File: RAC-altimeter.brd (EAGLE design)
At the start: 160 x 100 mm, 30 parts, among them J3 CORTEX_DEBUG_SMD, U1 MAX32660GTP+, U2 BMI088, U3 BMP388, U4 W25N01GVZEIG_TR, Y1 32.768kHz

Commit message: Organized board for layout
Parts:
- moved R2 104.5 mm to (62.2, 27.9)
- moved C2 103.2 mm to (54.6, 63.5)
- moved D1 101.7 mm to (61.0, 24.1)
- moved R1 100.5 mm to (62.2, 30.5)
- moved C1 98.8 mm to (54.6, 61.0)
- moved U1 95.2 mm to (53.3, 25.4)
- moved U3 95.2 mm to (59.7, 62.2)
- moved Y1 91.5 mm to (57.1, 34.3)
- moved R6 90.0 mm to (59.7, 66.0)
- moved U4 89.8 mm to (52.1, 5.08)
- moved R4 87.3 mm to (67.3, 27.9)
- moved C8 86.8 mm to (48.3, 10.2)
- moved R5 86.0 mm to (61.0, 21.6)
- moved R3 83.2 mm to (67.3, 30.5)
- moved C4 82.7 mm to (62.2, 52.1)
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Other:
- board size 160 x 100 mm -> 25.4 x 50.8 mm

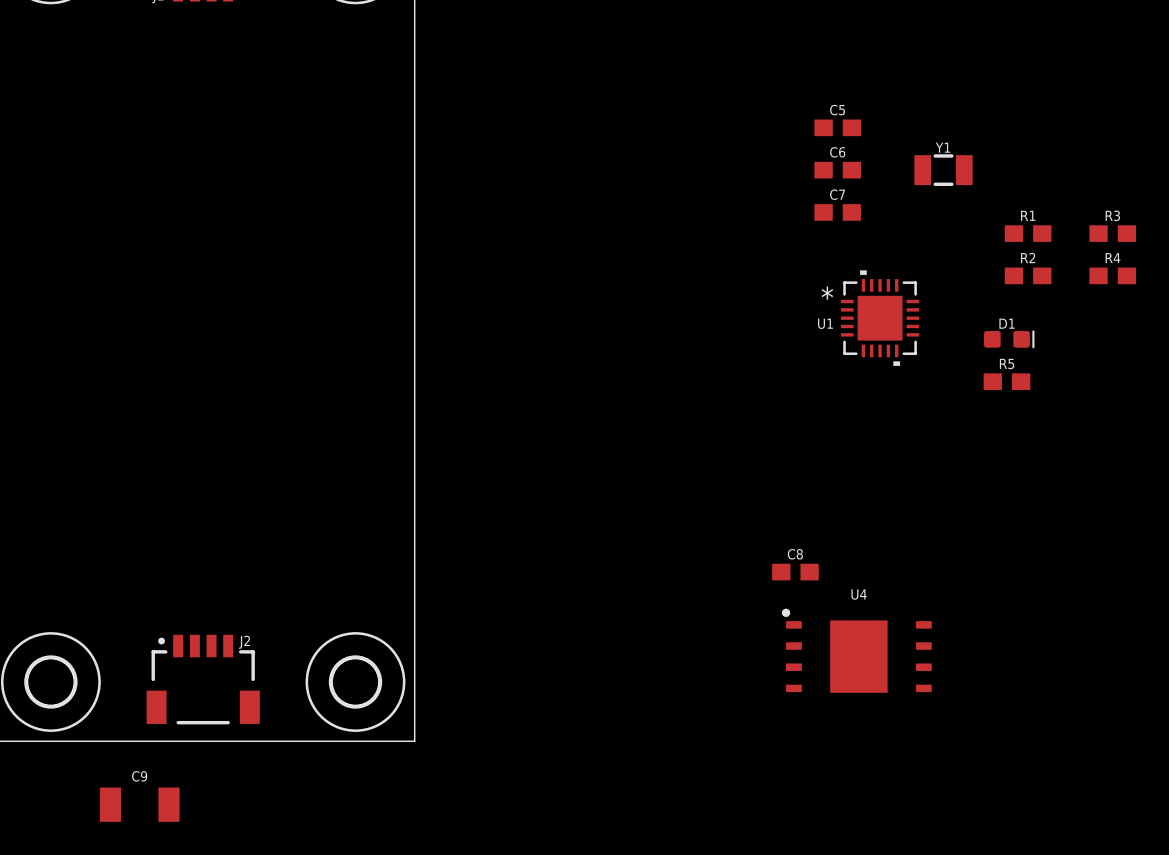
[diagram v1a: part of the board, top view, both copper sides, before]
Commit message: Swapped I2C0 and I2C1 bus connections for better routing
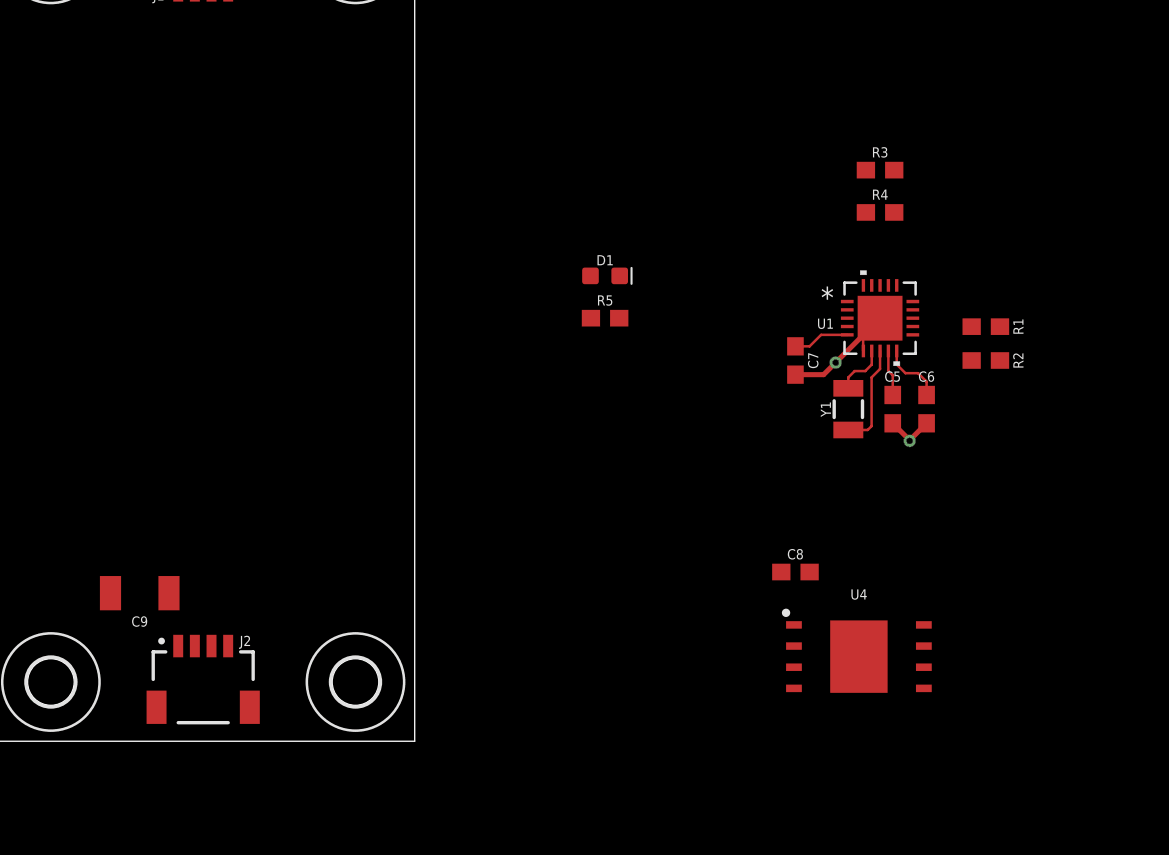
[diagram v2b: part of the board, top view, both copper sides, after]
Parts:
- moved D1 24.4 mm to (36.8, 27.9)
- moved R5 24.4 mm to (36.8, 25.4)
- moved C5 17.2 mm to (54.1, 19.9), turned to 270 degrees
- moved Y1 15.4 mm to (51.4, 19.9), turned to 90 degrees
- moved C6 15.3 mm to (56.1, 19.9), turned to 270 degrees
- moved R3 14.5 mm to (53.3, 34.3)
- moved R4 14.5 mm to (53.3, 31.8)
- moved C9 12.7 mm to (8.89, 8.89), turned to 180 degrees
- moved C7 9.25 mm to (48.3, 22.9), turned to 270 degrees
- moved R1 6.14 mm to (59.7, 24.9)
- moved R2 5.68 mm to (59.7, 22.9)
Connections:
- net I2C0_SCL: now also J1.4, J2.4; no longer U2.8, U3.2
- net I2C0_SDA: now also J1.3, J2.3; no longer U2.9, U3.4
- net I2C1_SCL: now also U2.8, U3.2; no longer J1.4, J2.4
- net I2C1_SDA: now also U2.9, U3.4; no longer J1.3, J2.3
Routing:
- net GND: track 0.00 -> 11.9 mm, vias 0 -> 2
- net 32KIN: track 0.00 -> 6.21 mm
- net VCORE: track 0.00 -> 3.83 mm
- net !RSTN: track 0.00 -> 3.40 mm
- net 32KOUT: track 0.00 -> 3.20 mm
- net VCC: track 0.00 -> 2.75 mm

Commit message: Partially routed board
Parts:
- moved R6 65.0 mm to (8.00, 26.7), turned to 90 degrees
- moved U3 64.8 mm to (5.33, 26.9), turned to 90 degrees
- moved C2 63.7 mm to (2.67, 26.7), turned to 270 degrees
- moved C1 58.4 mm to (5.33, 29.6)
- moved C4 55.1 mm to (8.89, 38.1), turned to 270 degrees
- moved C3 48.6 mm to (16.5, 38.1), turned to 270 degrees
- moved J4 46.4 mm to (26.7, 14.1), turned to 270 degrees
- moved U2 45.4 mm to (12.7, 38.1), turned to 270 degrees
- moved U4 42.1 mm to (15.2, 25.4)
- moved Y1 39.6 mm to (12.4, 12.8), turned to 180 degrees
- moved U1 38.9 mm to (15.2, 17.8)
- moved C7 38.7 mm to (10.2, 16.1)
- moved C5 38.4 mm to (16.5, 12.3)
- moved C6 38.2 mm to (18.7, 12.3)
- moved C8 36.8 mm to (17.1, 29.7), turned to 180 degrees
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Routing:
- net I2C0_SCL: track 0.00 -> 63.5 mm, vias 0 -> 3
- net I2C0_SDA: track 0.00 -> 55.5 mm, vias 0 -> 3
- net GND: track 11.9 -> 48.8 mm, vias 2 -> 12
- net VCC: track 2.75 -> 19.5 mm
- net !RSTN: track 3.40 -> 17.9 mm
- net !SPI0_CS: track 0.00 -> 14.3 mm, vias 0 -> 2
- net SPI0_MISO: track 0.00 -> 9.22 mm
- net SPI0_SCK: track 0.00 -> 8.88 mm
- net SWDCLK: track 0.00 -> 7.54 mm, vias 0 -> 2
- net UART1_TX: track 0.00 -> 7.52 mm, vias 0 -> 1
- net SWDIO: track 0.00 -> 7.01 mm
- net UART1_RX: track 0.00 -> 5.70 mm
- net SPI0_MOSI: track 0.00 -> 5.65 mm
- net 32KOUT: track 3.20 -> 5.94 mm
- net BMP_CS: track 0.00 -> 2.26 mm
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
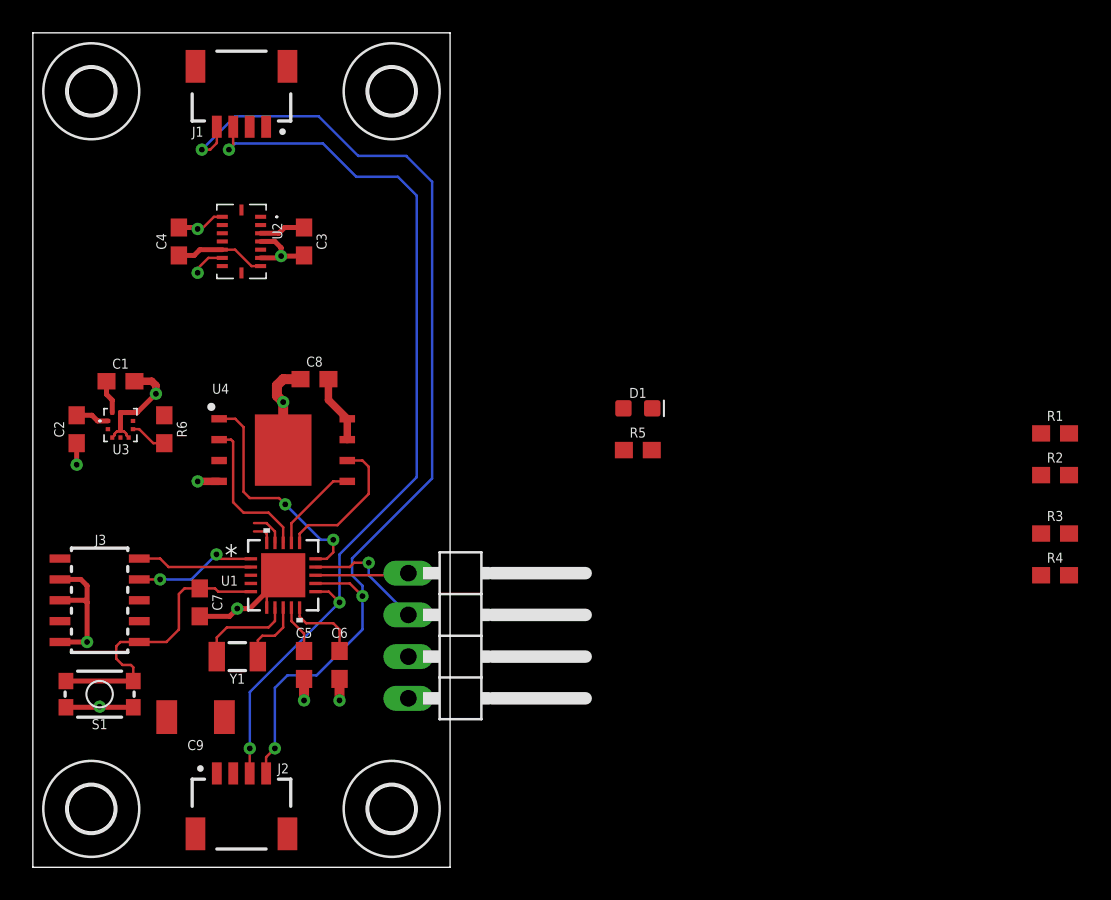
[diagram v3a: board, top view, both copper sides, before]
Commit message: Completely routed board
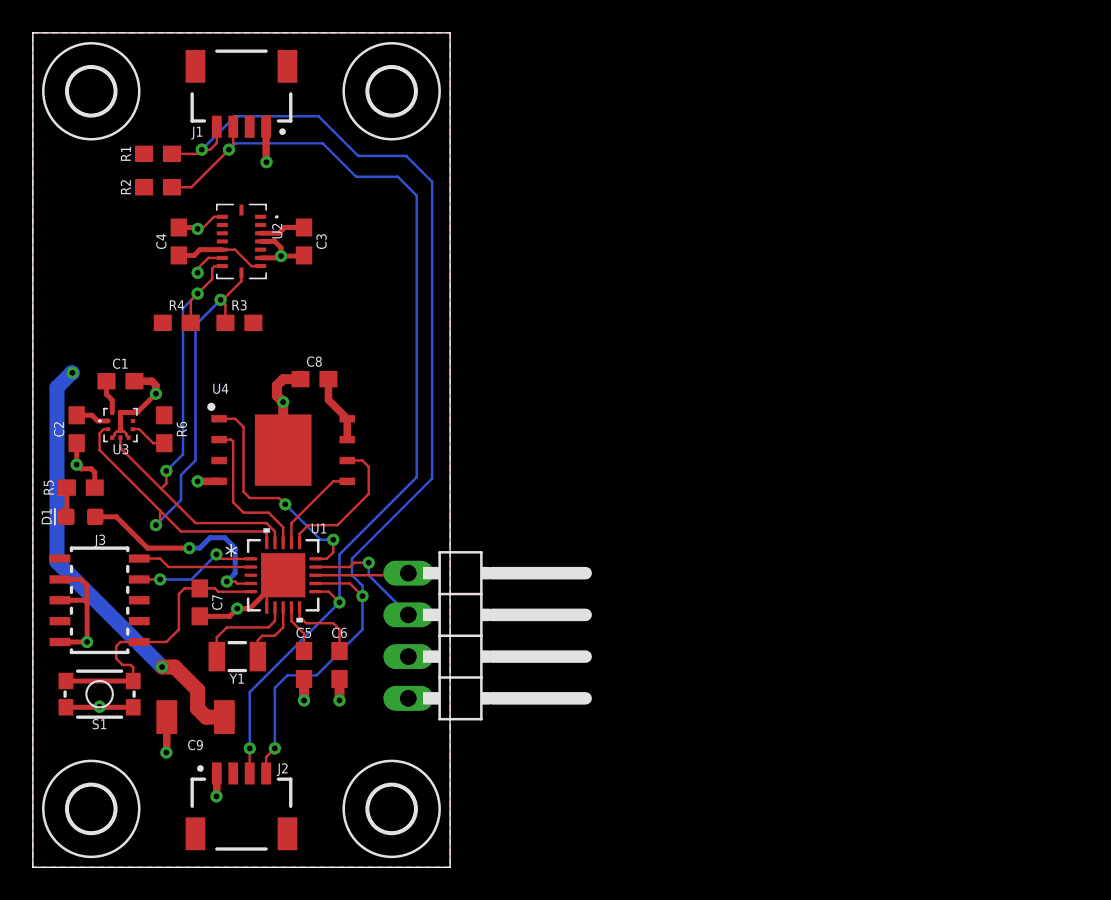
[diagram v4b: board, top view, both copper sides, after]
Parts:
- moved R2 57.4 mm to (7.62, 41.4), turned to 180 degrees
- moved R1 57.2 mm to (7.62, 43.4), turned to 180 degrees
- moved R4 55.6 mm to (8.76, 33.1), turned to 180 degrees
- moved R3 51.3 mm to (12.6, 33.1)
- moved D1 34.5 mm to (2.92, 21.3), turned to 180 degrees
- moved R5 34.0 mm to (2.92, 23.1)
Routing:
- net I2C1_SCL: track 1.39 -> 34.6 mm, vias 0 -> 2
- net I2C1_SDA: track 2.18 -> 30.2 mm, vias 0 -> 2
- net VCC: track 19.5 -> 46.2 mm, vias 0 -> 2
- net IO_LED: track 0.00 -> 13.6 mm, vias 0 -> 2
- net GND: track 48.8 -> 57.0 mm, vias 12 -> 15
- net I2C0_SDA: track 55.5 -> 59.9 mm
- net I2C0_SCL: track 63.5 -> 65.5 mm
- net LED_CATH: track 0.00 -> 1.79 mm
- added copper zone on layer 16, net GND
- added copper zone on layer 1, net VCC

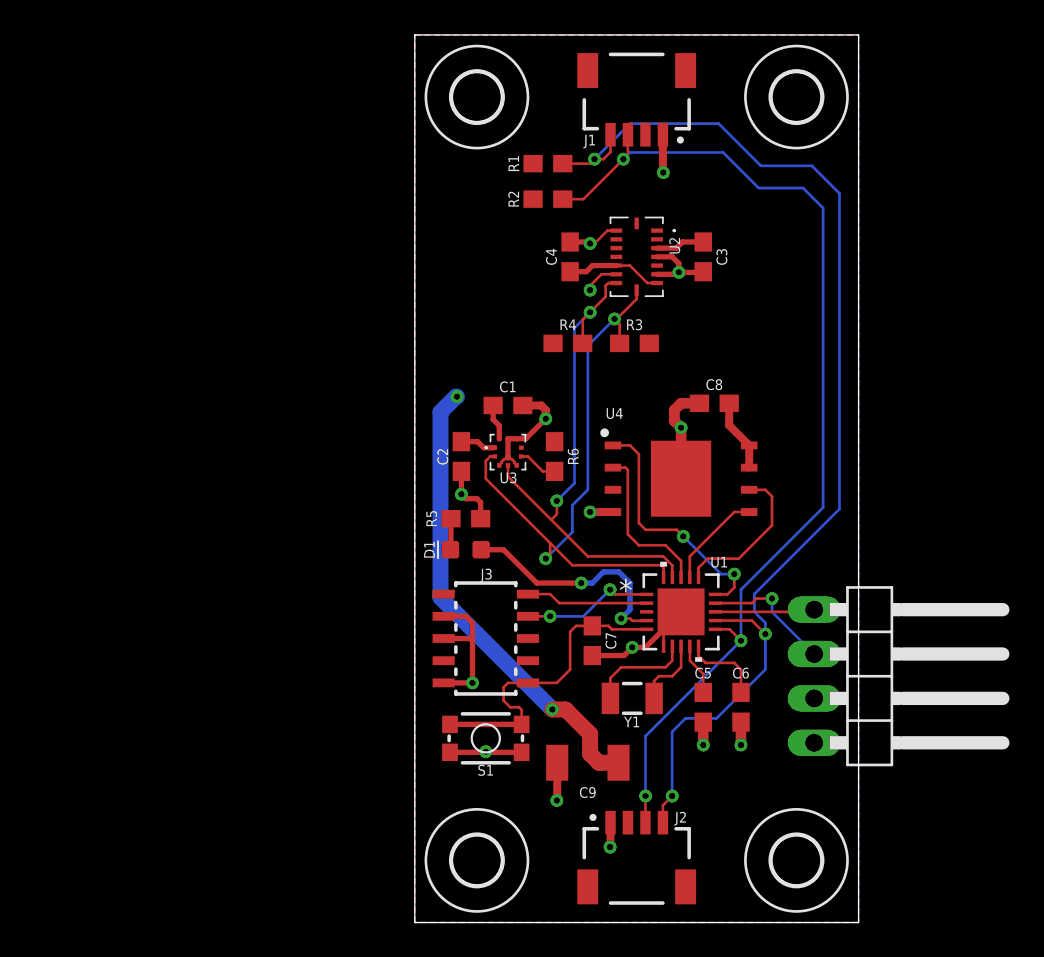
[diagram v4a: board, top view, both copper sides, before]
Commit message: Removed spare JST connector and BMP388 capacitor; redid IC placement
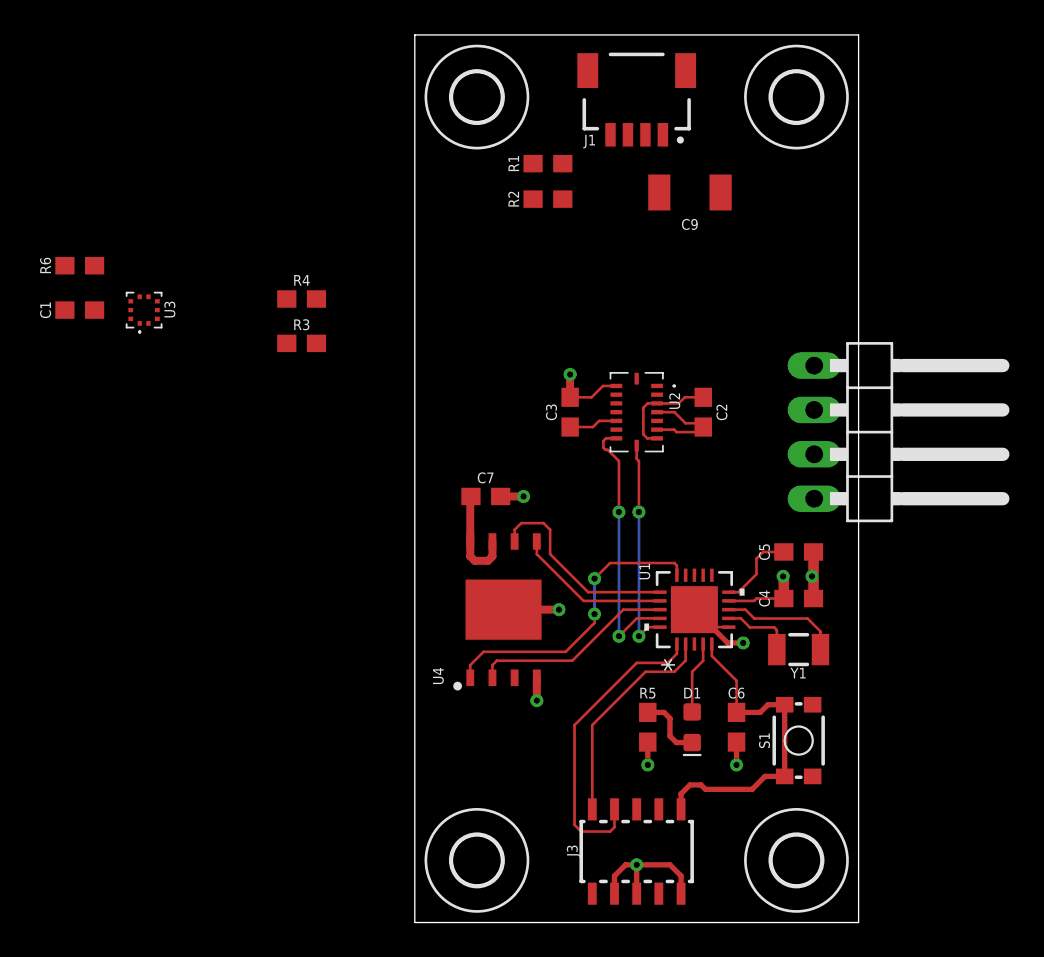
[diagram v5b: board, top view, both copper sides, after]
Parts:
- removed C8: 10uF, SparkFun-Capacitors:0603
- removed J2: (no value), SparkFun-Connectors:JST04_1MM_RA
- C4: value 0.1uF -> 1.0uF
- C6: value 1.0uF -> 0.1uF
- C7: value 0.1uF -> 10uF
- moved C9 33.2 mm to (15.7, 41.8), turned to 0 degrees
- moved R6 29.3 mm to (-19.2, 37.6), turned to 180 degrees
- moved C1 25.1 mm to (-19.2, 35.1), turned to 180 degrees
- moved C4 23.5 mm to (22.0, 18.5), turned to 0 degrees
- moved U3 22.4 mm to (-15.5, 35.1), turned to 180 degrees
- moved R3 19.1 mm to (-6.48, 33.1)
- moved S1 17.9 mm to (22.0, 10.4), turned to 270 degrees
- moved D1 16.5 mm to (15.9, 11.2), turned to 270 degrees
- moved R5 15.8 mm to (13.3, 11.2), turned to 270 degrees
- moved R4 15.5 mm to (-6.48, 35.7)
- moved J3 14.9 mm to (12.7, 4.06), turned to 0 degrees
- moved C2 14.1 mm to (16.5, 29.2)
- moved J4 14.0 mm to (26.7, 28.1)
- moved U4 12.6 mm to (5.08, 17.9), turned to 90 degrees
- moved C3 11.7 mm to (8.89, 29.2)
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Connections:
- net !RSTN: now also C6.1; no longer C7.1
- net GND: now also C3.1, C4.2; no longer C3.2, C4.1, C8.2, J2.1
- net I2C0_SCL: no longer J2.4
- net I2C0_SDA: no longer J2.3
- net VCC: now also C3.2, C4.1, C7.1; no longer C3.1, C4.2, C5.1, C8.1, J2.2
- net VCORE: now also C5.1; no longer C6.1
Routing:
- net I2C0_SCL: track 65.5 -> 0.00 mm, vias 3 -> 0
- net I2C0_SDA: track 59.9 -> 0.00 mm, vias 3 -> 0
- net VCC: track 46.2 -> 19.1 mm, vias 2 -> 1
- net I2C1_SCL: track 34.6 -> 12.4 mm
- net GND: track 57.0 -> 35.2 mm, vias 15 -> 9
- net I2C1_SDA: track 30.2 -> 15.2 mm
- net SWDCLK: track 7.54 -> 17.4 mm, vias 2 -> 0
- net IO_LED: track 13.6 -> 4.15 mm, vias 2 -> 0
- net UART1_TX: track 7.52 -> 0.00 mm, vias 1 -> 0
- net UART1_RX: track 5.70 -> 0.00 mm
- net SWDIO: track 7.01 -> 12.6 mm
- net SPI0_MOSI: track 5.65 -> 8.88 mm
- net !SPI0_CS: track 14.3 -> 17.1 mm
- net 32KIN: track 4.07 -> 6.80 mm
- net SPI0_SCK: track 8.88 -> 11.6 mm
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- removed copper zone on layer 16, net GND
- removed copper zone on layer 1, net VCC
